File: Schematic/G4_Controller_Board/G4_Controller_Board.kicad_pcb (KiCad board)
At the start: 2 copper layers, 126.4 x 40.6 mm, 39 parts, among them J10 Solenoid, J11 Inter-board Jumper, J12 Inter-board Jumper, J15 IR LED Rec., J16 IR LED Emitter, J17 Positive BUS, J18 Negative BUS, J2 ESC Right, J3 ESC Left, J6 Rev Trigger (Optional), J7 Fire Trigger, J8 Magazine Removal Trigger, J9 I2C Out, Q1 2N7000, Q2 Q_NMOS_GDS, Q3 Q_PMOS_GDS, SW2 Preset A, SW3 Preset B, SW4 Preset C, SW7 RotaryEncoder_Switch, U1 ESP32-LOLIN32-Lite, U2 Mini360

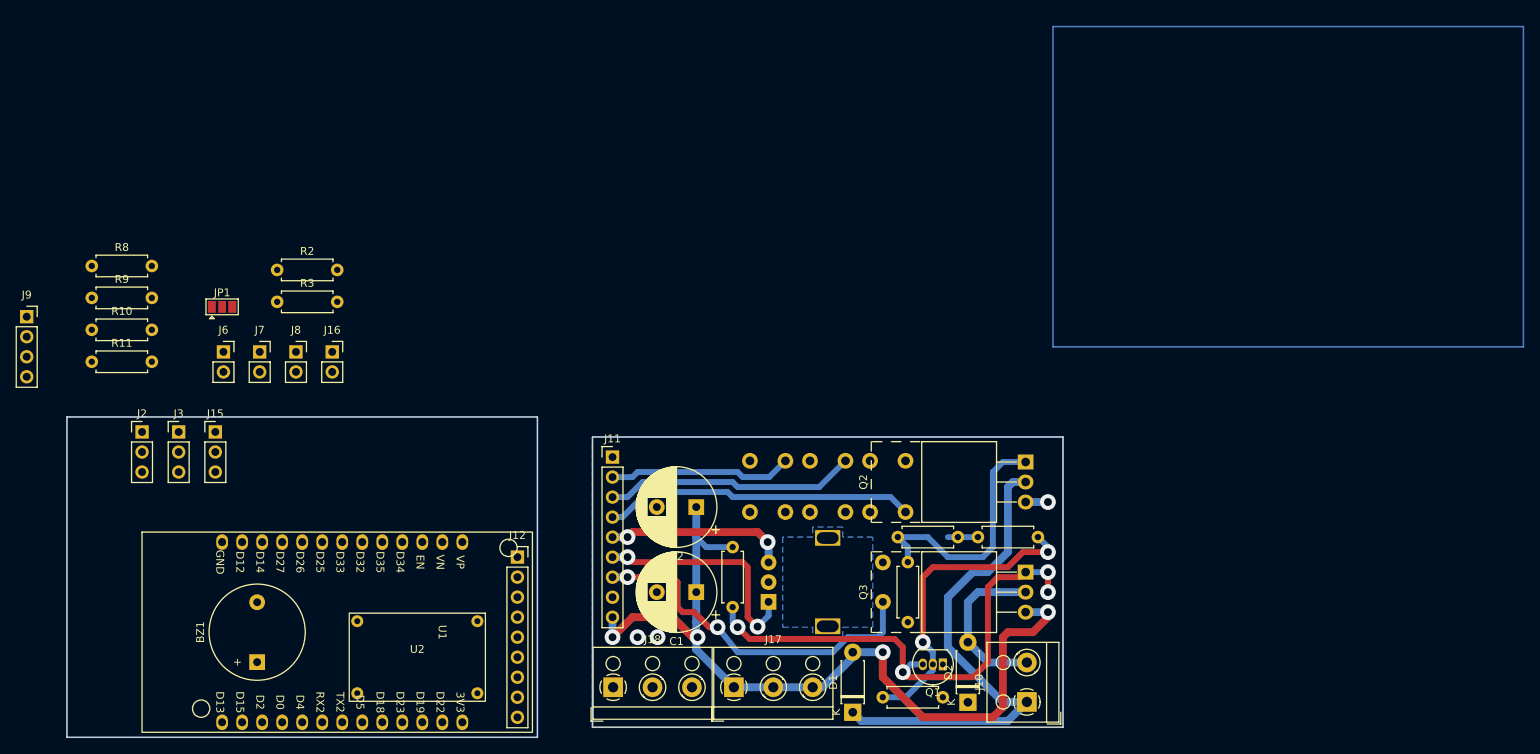
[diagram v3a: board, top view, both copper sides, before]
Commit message: update PCB model
progress on logic-side board
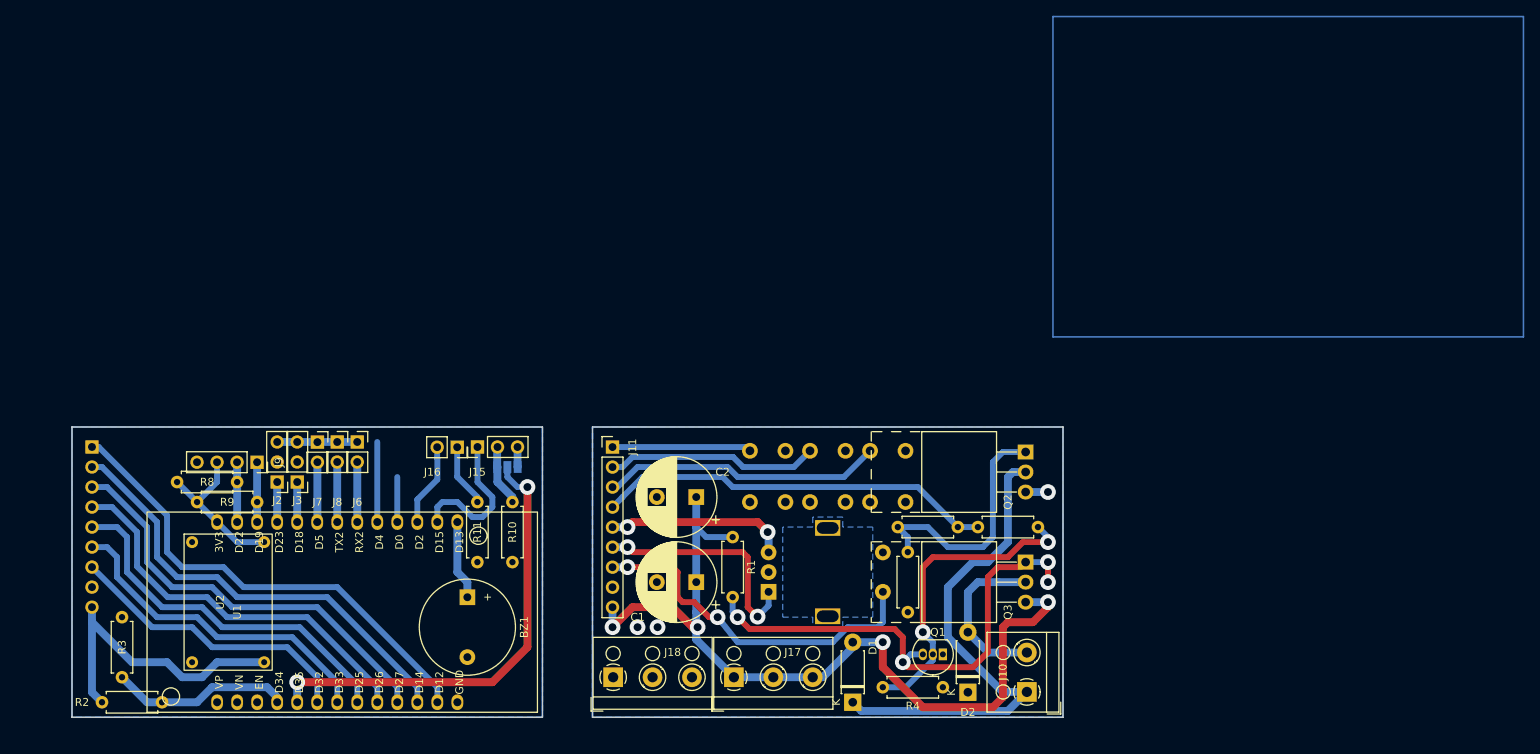
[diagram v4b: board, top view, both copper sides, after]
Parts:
- J12, JP1: moved to B.Cu
- moved R10 61.0 mm to (110.5, 88.3), turned to 90 degrees
- moved R2 56.8 mm to (66.0, 106.0), turned to 180 degrees
- moved J12 55.8 mm to (57.1, 73.7), turned to 180 degrees
- moved R11 55.1 mm to (106.0, 88.3), turned to 90 degrees
- moved R3 44.6 mm to (61.0, 95.2), turned to -90 degrees
- moved JP1 41.5 mm to (109.9, 76.2)
- moved J9 34.6 mm to (78.1, 75.6), turned to -90 degrees
- moved J15 33.3 mm to (106.1, 73.7), turned to 90 degrees
- moved R8 29.5 mm to (67.9, 78.1)
- moved R9 29.1 mm to (70.5, 80.6)
- moved BZ1 27.9 mm to (104.8, 92.7), turned to -90 degrees
- moved U2 25.0 mm to (74.4, 93.3), turned to 90 degrees
- moved J6 20.5 mm to (90.8, 73.0)
- moved J16 19.9 mm to (103.5, 73.7), turned to -90 degrees
- moved J2 18.3 mm to (80.6, 78.1), turned to 180 degrees
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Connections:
- J11 pad 1: /Pusher Pin -> /Preset C
- J11 pad 2: /Preset C -> /Preset B
- J11 pad 3: /Preset B -> /Preset A
- J11 pad 4: /Preset A -> /Pusher Pin
- J12 pad 1: /Pusher Pin -> /Preset C
- J12 pad 2: /Preset C -> /Preset B
- J12 pad 3: /Preset B -> /Preset A
- J12 pad 4: /Preset A -> /Pusher Pin
- SW2 pad 1: GND -> /Preset A
- SW2 pad 2: /Preset A -> GND
- SW3 pad 1: GND -> /Preset B
- SW3 pad 2: /Preset B -> GND
- SW4 pad 1: GND -> /Preset C
- SW4 pad 2: /Preset C -> GND
- SW7 pad MP: Tab -> (no net)
- U1 pad 12: /IR Rec. Supply -> /Encoder Switch
- U1 pad 13: /IR Emitter -> /Encoder A
- U1 pad 14: /Pusher Pin -> /Encoder B
- U1 pad 15: /Preset C -> /Pusher Pin
- U1 pad 16: /Preset B -> /Preset A
- U1 pad 17: /Preset A -> /Preset B
- U1 pad 18: /Buzzer -> /Preset C
- U1 pad 20: /Encoder Switch -> /Buzzer
- U1 pad 21: /Encoder B -> /IR Rec. Supply
- U1 pad 22: /Encoder A -> /IR Emitter
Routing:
- net /Pusher Pin: track 3.81 -> 100.7 mm
- net /IR Reciever: track 0.00 -> 58.2 mm, vias 0 -> 2
- net /Preset C: track 23.3 -> 78.7 mm
- net /Preset B: track 32.0 -> 84.3 mm
- net /Preset A: track 39.5 -> 89.4 mm
- net /Encoder B: track 23.0 -> 69.8 mm
- net /Encoder A: track 29.5 -> 71.7 mm
- net +12V: track 106.5 -> 144.6 mm
- net /Encoder Switch: track 45.9 -> 83.4 mm
- net /Battery Reader: track 0.00 -> 23.0 mm
- net +3V3: track 0.00 -> 20.3 mm
- net /IR Rec. Supply: track 0.00 -> 18.9 mm
- net /IR Emitter: track 0.00 -> 11.2 mm
- net GND: track 2.84 -> 13.0 mm
- net /SolenoidTrig A: track 0.00 -> 10.2 mm
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- added copper zone on B.Cu, net (none)
- removed copper zone on B.Cu, net Tab
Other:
- board size 126.4 x 40.6 mm -> 125.7 x 36.8 mm

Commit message: try 3 flywheel mount
tried single piece flywheel mount, but that resulted in print issues, so I'm trying a different method that uses more bolts. Also updated other things such as the PCB.
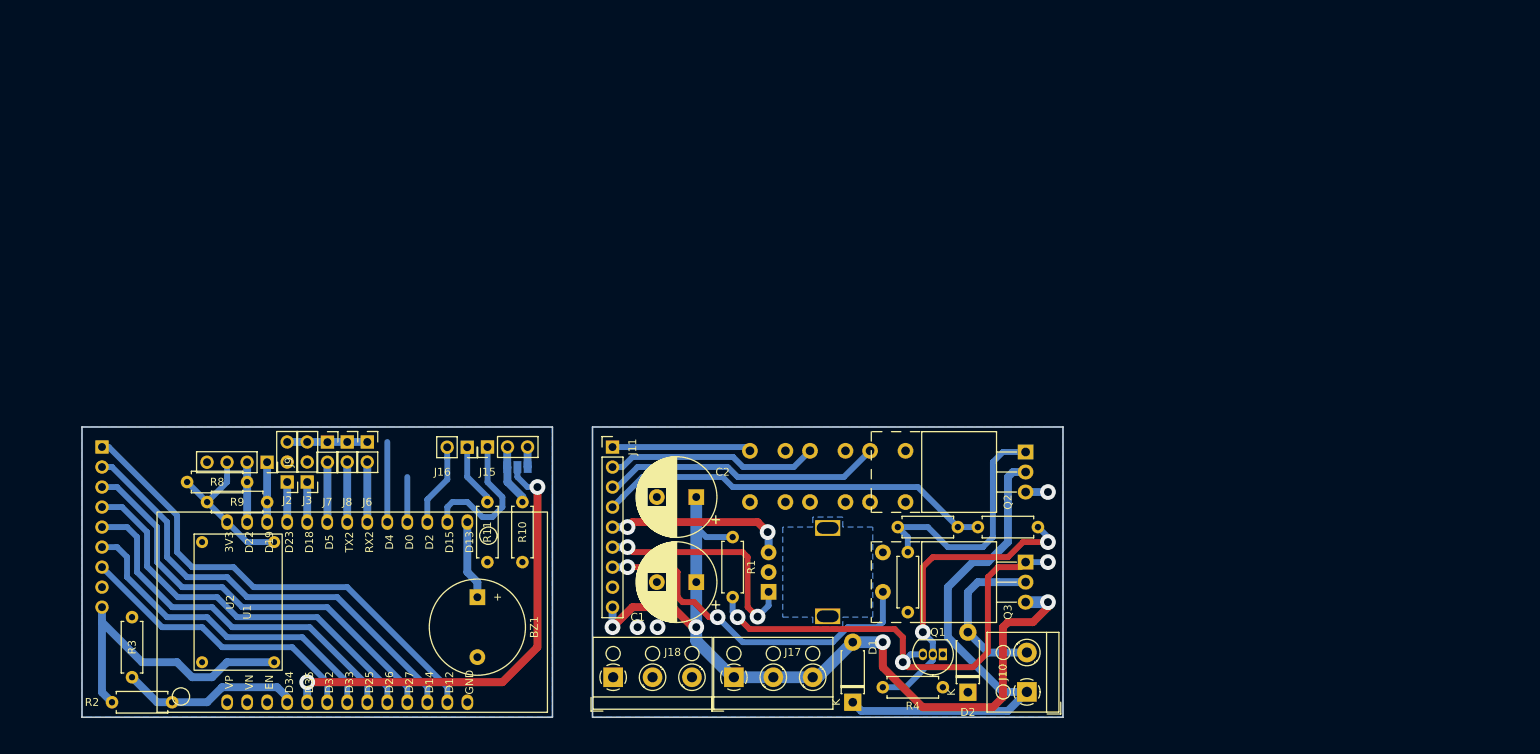
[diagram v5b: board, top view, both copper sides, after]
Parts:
- moved J2 1.27 mm to (81.9, 78.1)
- moved R10 1.27 mm to (111.8, 88.3)
- moved R8 1.27 mm to (69.2, 78.1)
- moved J12 1.27 mm to (58.4, 73.7)
- moved BZ1 1.27 mm to (106.0, 92.7)
- moved J15 1.27 mm to (107.3, 73.7)
- moved J16 1.27 mm to (104.8, 73.7)
- moved J3 1.27 mm to (84.5, 78.1)
- moved J6 1.27 mm to (92.1, 73.0)
- moved J7 1.27 mm to (87.0, 73.0)
- moved J8 1.27 mm to (89.5, 73.0)
- moved J9 1.27 mm to (79.4, 75.6)
- moved JP1 1.27 mm to (111.1, 76.2)
- moved R11 1.27 mm to (107.3, 88.3)
- moved R2 1.27 mm to (67.3, 106.0)
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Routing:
- net Net-(Q1-D): track 63.3 -> 60.7 mm, vias 4 -> 3
- net /Encoder Switch: track 83.4 -> 82.8 mm
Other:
- board size 125.7 x 36.8 mm -> 124.5 x 36.8 mm
- board text removed: "Side 1"
- board text removed: "Side 2"

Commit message: update PCB
prototype revision should be completed
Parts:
- removed the J6 at (92.1, 73.0)
- added J12: SolenoidTrig A (Optional), Connector_PinHeader_2.54mm:PinHeader_1x03_P2.54mm_Vertical, F.Cu at (93.3, 76.8)
- added J13: SolenoidTrig B (Optional), Connector_PinHeader_2.54mm:PinHeader_1x03_P2.54mm_Vertical, F.Cu at (95.9, 76.8)
- added J9: Magazine Removal Trigger, Connector_PinHeader_2.54mm:PinHeader_1x03_P2.54mm_Vertical, F.Cu at (88.3, 76.8)
- D1, D2: value DIODE -> 1N4001
- J11: value Inter-board Jumper -> Board Interconnect; footprint Connector_PinHeader_2.54mm:PinHeader_1x09_P2.54mm_Vertical -> Connector_PinSocket_2.54mm:PinSocket_1x09_P2.54mm_Vertical
- J14: renamed from J12; value Inter-board Jumper -> Board Interconnect; footprint Connector_PinSocket_2.54mm:PinSocket_1x09_P2.54mm_Vertical -> Connector_PinHeader_2.54mm:PinHeader_1x09_P2.54mm_Vertical
- J18: renamed from J16; footprint Connector_PinSocket_2.54mm:PinSocket_1x02_P2.54mm_Vertical -> Connector_PinHeader_2.54mm:PinHeader_1x02_P2.54mm_Vertical
- J6: renamed from J9; footprint Connector_PinSocket_2.54mm:PinSocket_1x04_P2.54mm_Vertical -> Connector_PinHeader_2.54mm:PinHeader_1x04_P2.54mm_Vertical
- J7: value Fire Trigger -> Rev Trigger (Optional); footprint Connector_PinSocket_2.54mm:PinSocket_1x02_P2.54mm_Vertical -> Connector_PinHeader_2.54mm:PinHeader_1x03_P2.54mm_Vertical
- J8: value Magazine Removal Trigger -> Fire Trigger; footprint Connector_PinSocket_2.54mm:PinSocket_1x02_P2.54mm_Vertical -> Connector_PinHeader_2.54mm:PinHeader_1x03_P2.54mm_Vertical
- moved D1 8.89 mm to (153.7, 97.2), turned to -90 degrees
- moved D2 8.89 mm to (168.3, 95.9), turned to -90 degrees
- moved J8 5.38 mm to (85.7, 76.8), turned to 180 degrees
- moved J7 5.36 mm to (90.8, 76.8), turned to 180 degrees
- moved J2 1.80 mm to (80.6, 76.8)
- moved R8 1.80 mm to (67.9, 76.8)
- moved J3 1.80 mm to (83.2, 76.8)
- moved J6 1.80 mm to (78.1, 74.3)
- moved R10 1.80 mm to (110.5, 87.0)
- moved J14 1.80 mm to (57.1, 72.4)
- moved BZ1 1.80 mm to (104.8, 91.5)
- moved J17 1.80 mm to (106.1, 72.4)
- moved J18 1.80 mm to (103.5, 72.4)
- moved JP1 1.80 mm to (109.9, 74.9)
- moved R11 1.80 mm to (106.0, 87.0)
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- renumbered J15 to J17, J17 to J19, J18 to J20
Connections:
- D1 pad 1: /SOLENOID_A -> +12V
- D1 pad 2: +12V -> /SOLENOID_A
- D2 pad 1: GND -> /SOLENOID_B
- D2 pad 2: /SOLENOID_B -> GND
- J2 pad 2: unconnected-(J2-Pin_2-Pad2) -> GND
- J3 pad 2: unconnected-(J3-Pin_2-Pad2) -> GND
- J7 pad 1: GND -> /RevTrg
- J7 pad 2: /FireTrg -> GND
- J8 pad 1: GND -> /FireTrg
- J8 pad 2: /MagTrg -> GND
- SW7 pad MP: (no net) -> Tab
- U1 pad 23: /SolenoidTrig B -> /SolTrig B
- U1 pad 24: /SolenoidTrig A -> /SolTrig A
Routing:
- net GND: track 13.0 -> 38.7 mm
- net /SolenoidTrig A: track 10.2 -> 0.00 mm
- net /SolenoidTrig B: track 5.72 -> 0.00 mm
- net /SolTrig B: track 0.00 -> 5.08 mm
- net /SolTrig A: track 0.00 -> 5.08 mm
- net /RevTrg: track 7.62 -> 5.08 mm
- net /MagTrg: track 7.62 -> 5.08 mm
- net /FireTrg: track 7.61 -> 5.12 mm
- net Tab: track 0.00 -> 0.90 mm
- net (no net): track 0.90 -> 0.00 mm
- added copper zone on B.Cu, net Tab
- removed copper zone on B.Cu, net (none)
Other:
- board size 124.5 x 36.8 mm -> 125.7 x 36.8 mm
